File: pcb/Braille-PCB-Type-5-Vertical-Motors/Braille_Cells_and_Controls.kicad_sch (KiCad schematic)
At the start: 6 parts, among them U26 74HC595, U27 74HC595, U28 74HC595, U29 74HC595, U30 74HC595, U31 74HC595

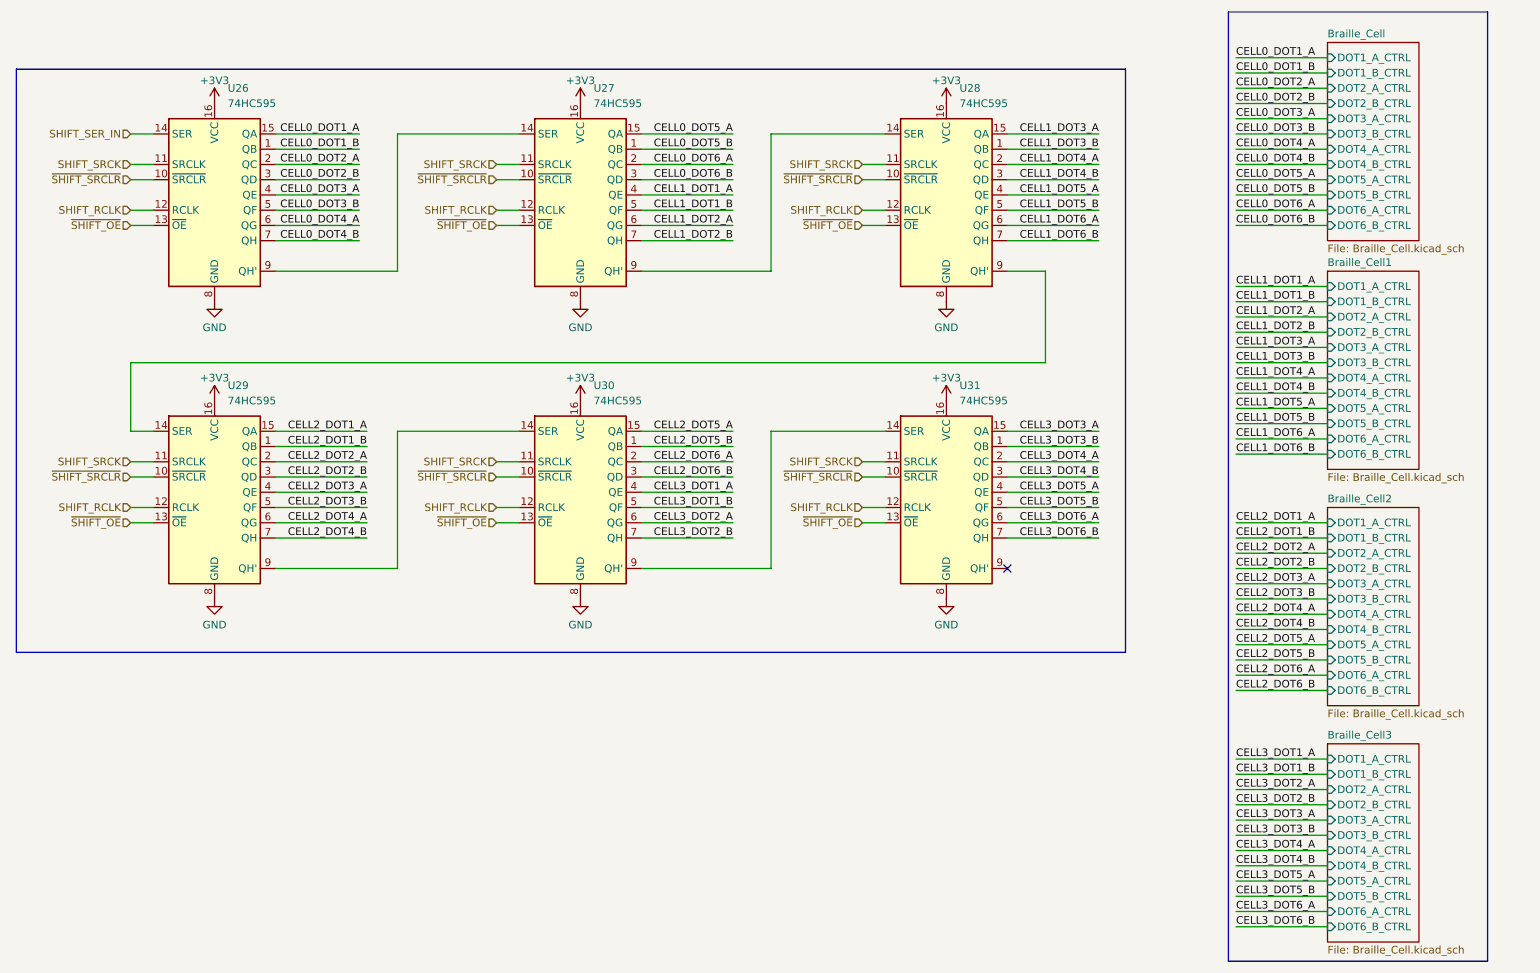
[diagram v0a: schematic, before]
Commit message: PCB: Update to have 3 motors, dimensioned layout template
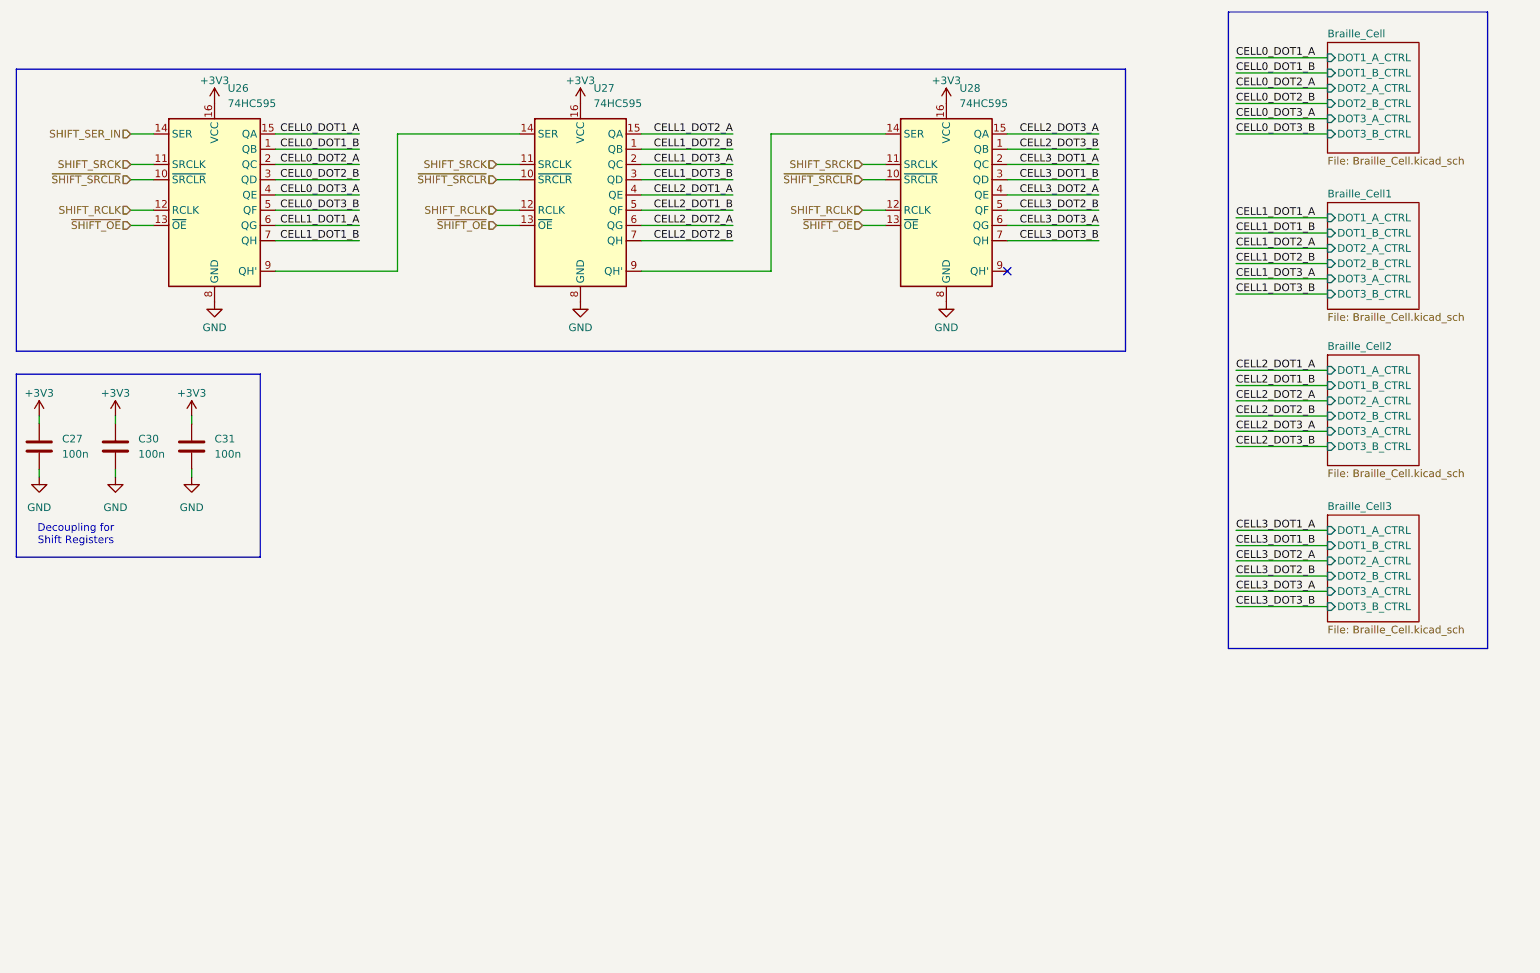
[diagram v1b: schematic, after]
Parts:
- removed U29, U30, U31: 74HC595, Package_SO:SOP-16_3.9x9.9mm_P1.27mm, symbol 74xx:74HC595
- added C27, C30, C31: 100n, Capacitor_SMD:C_0603_1608Metric_Pad1.08x0.95mm_HandSolder, symbol Device:C
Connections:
- net CELL0_DOT4_A is gone; now on net CELL1_DOT1_A: U26.6 (QG)
- net CELL0_DOT4_B is gone; now on net CELL1_DOT1_B: U26.7 (QH)
- net CELL0_DOT5_A is gone; now on net CELL1_DOT2_A: U27.15 (QA)
- net CELL0_DOT5_B is gone; now on net CELL1_DOT2_B: U27.1 (QB)
- net CELL0_DOT6_A is gone; now on net CELL1_DOT3_A: U27.2 (QC)
- net CELL0_DOT6_B is gone; now on net CELL1_DOT3_B: U27.3 (QD)
- net CELL1_DOT4_A is gone; now on net CELL3_DOT1_A: U28.2 (QC)
- net CELL1_DOT4_B is gone; now on net CELL3_DOT1_B: U28.3 (QD)
- net CELL1_DOT5_A is gone; now on net CELL3_DOT2_A: U28.4 (QE)
- net CELL1_DOT5_B is gone; now on net CELL3_DOT2_B: U28.5 (QF)
- net CELL1_DOT6_A is gone; now on net CELL3_DOT3_A: U28.6 (QG)
- net CELL1_DOT6_B is gone; now on net CELL3_DOT3_B: U28.7 (QH)
- net +3V3: now also C27.1, C30.1, C31.1
- net CELL1_DOT1_A: no longer U27.4 (QE)
- net CELL1_DOT1_B: no longer U27.5 (QF)
- net CELL1_DOT2_A: no longer U27.6 (QG)
- net CELL1_DOT2_B: no longer U27.7 (QH)
- net CELL1_DOT3_A: no longer U28.15 (QA)
- net CELL1_DOT3_B: no longer U28.1 (QB)
- net CELL2_DOT1_A: now also U27.4 (QE)
- net CELL2_DOT1_B: now also U27.5 (QF)
- net CELL2_DOT2_A: now also U27.6 (QG)
- net CELL2_DOT2_B: now also U27.7 (QH)
- net CELL2_DOT3_A: now also U28.15 (QA)
- net CELL2_DOT3_B: now also U28.1 (QB)
- net GND: now also C27.2, C30.2, C31.2
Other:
- sheet Braille_Cell ports: added none; removed DOT4_A_CTRL, DOT4_B_CTRL, DOT5_A_CTRL, DOT5_B_CTRL, DOT6_A_CTRL, DOT6_B_CTRL
- sheet Braille_Cell1 ports: added none; removed DOT4_A_CTRL, DOT4_B_CTRL, DOT5_A_CTRL, DOT5_B_CTRL, DOT6_A_CTRL, DOT6_B_CTRL
- sheet Braille_Cell2 ports: added none; removed DOT4_A_CTRL, DOT4_B_CTRL, DOT5_A_CTRL, DOT5_B_CTRL, DOT6_A_CTRL, DOT6_B_CTRL
- sheet Braille_Cell3 ports: added none; removed DOT4_A_CTRL, DOT4_B_CTRL, DOT5_A_CTRL, DOT5_B_CTRL, DOT6_A_CTRL, DOT6_B_CTRL
- note added: "Decoupling for Shift Registers"

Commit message: PCB: Add cross-PCB connectors
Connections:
- net SHIFT_SER_OUT: now reaches U28.9 (QH')
- no-connect marks 1 -> 0
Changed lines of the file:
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@@
 		(rev "Rev 2")
 	)
-	(no_connect
-		(at 185.42 55.88)
-	)
 	(wire
 		(pts
@@
 		(pts
 			(xy 36.83 80.01) (xy 36.83 81.28)
+		)
+		(stroke
+			(width 0)
+			(type default)
+		)
+	)
+	(wire
+		(pts
+			(xy 185.42 55.88) (xy 187.96 55.88)
 		)
 		(stroke
@@
 		)
 	)
+	(hierarchical_label "SHIFT_SER_OUT"
+		(shape output)
+		(at 187.96 55.88 0)
+		(fields_autoplaced yes)
+		(effects
+			(font
+				(size 1.27 1.27)
+			)
+			(justify left)
+		)
+	)
